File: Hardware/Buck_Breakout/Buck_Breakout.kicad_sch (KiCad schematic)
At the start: 7 parts, among them U1 AP62250WU

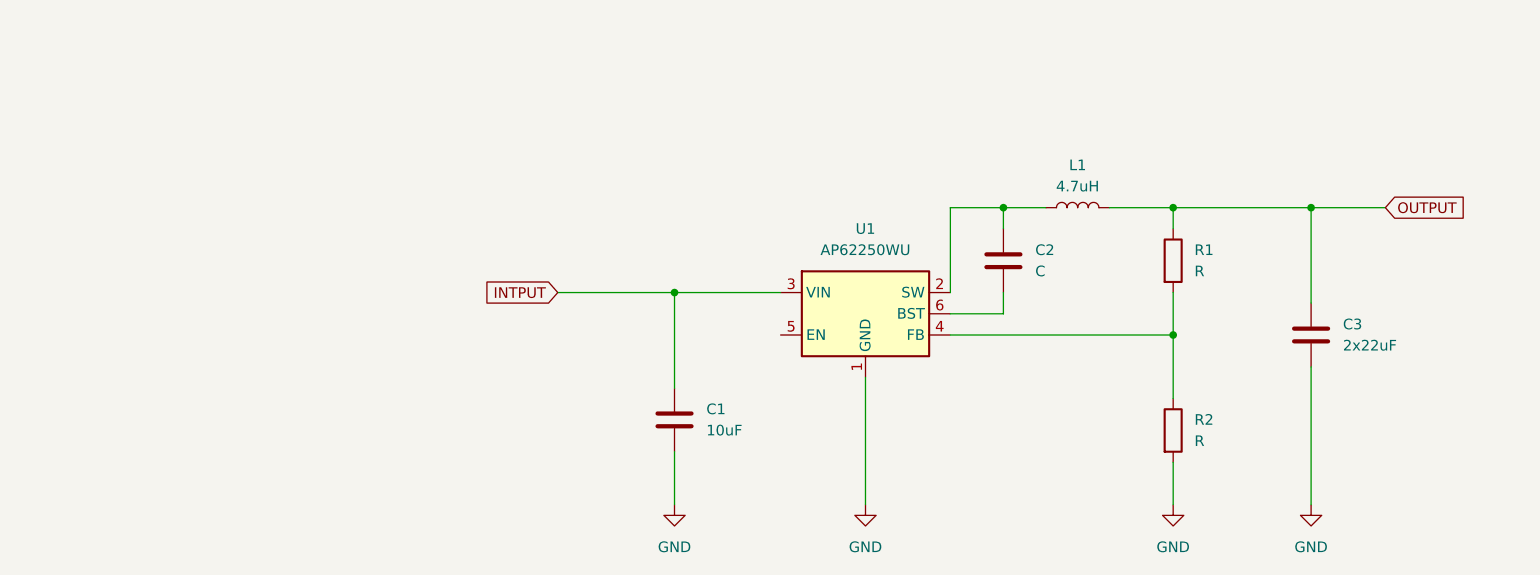
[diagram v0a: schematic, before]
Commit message: Finish Buck converter schematic and footprint assignments
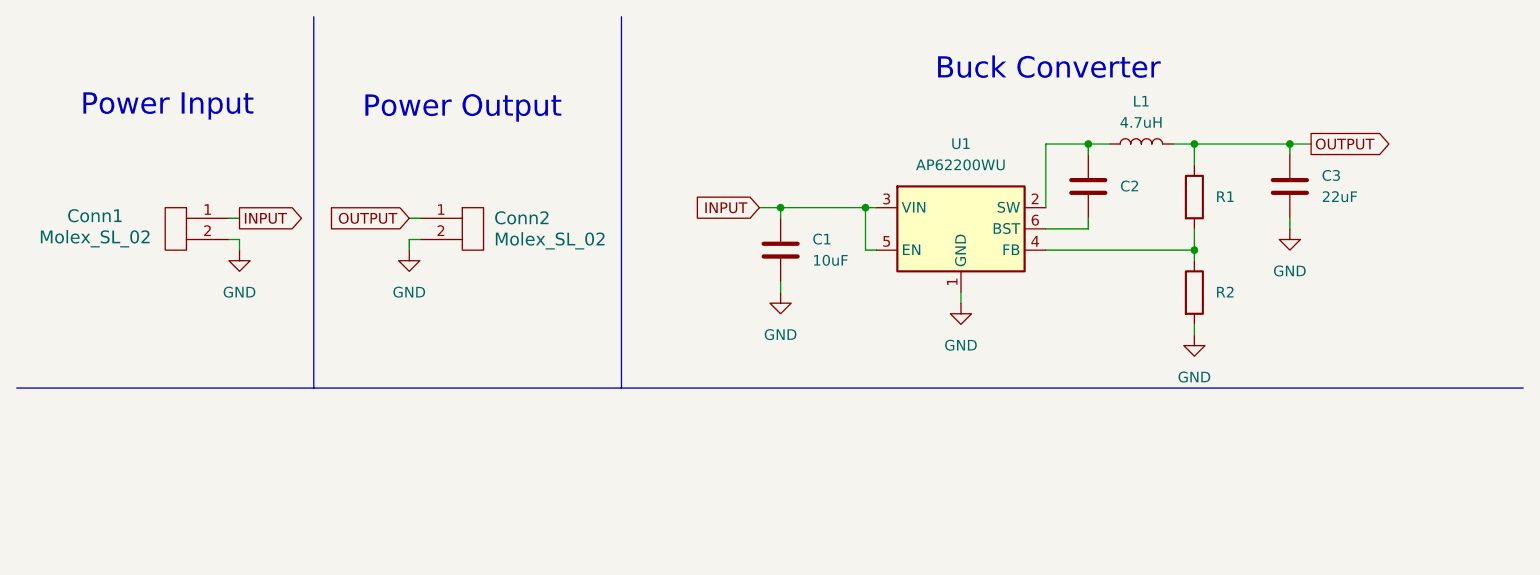
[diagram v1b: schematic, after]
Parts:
- added Conn1, Conn2: Molex_SL_02, MRDT_Connectors:MOLEX_SL_02_Vertical, symbol MRDT_Connectors:Molex_SL_02
- C1, C2: footprint (none) -> Capacitor_SMD:C_0603_1608Metric_Pad1.08x0.95mm_HandSolder
- C3: value 2x22uF -> 22uF; footprint (none) -> Capacitor_SMD:C_0603_1608Metric_Pad1.08x0.95mm_HandSolder
- L1: footprint (none) -> Inductor_SMD:L_1008_2520Metric_Pad1.43x2.20mm_HandSolder
- R1, R2: footprint (none) -> Resistor_SMD:R_0603_1608Metric_Pad0.98x0.95mm_HandSolder
- U1: value AP62250WU -> AP62200WU
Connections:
- net INTPUT is gone; now on net INPUT: C1.1, U1.3 (VIN)
- net GND: now also Conn1.2, Conn2.2
- net OUTPUT: now also Conn2.1
- net INPUT: now reaches U1.5 (EN)
- net INPUT: now also Conn1.1
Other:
- note added: "Buck Converter"
- note added: "Power Input"
- note added: "Power Output"
- moved on the sheet: C1, C2, C3, L1, R1, R2, U1

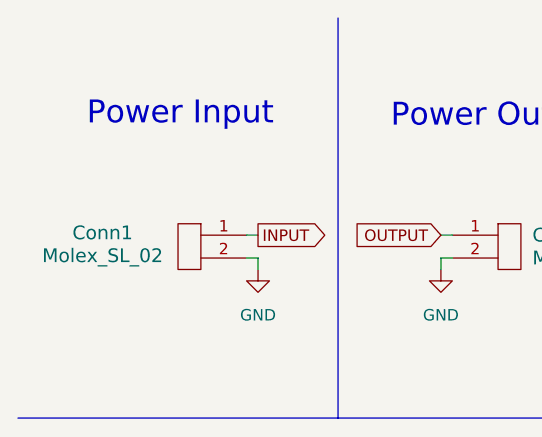
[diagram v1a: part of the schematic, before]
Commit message: Finish buck converter layout
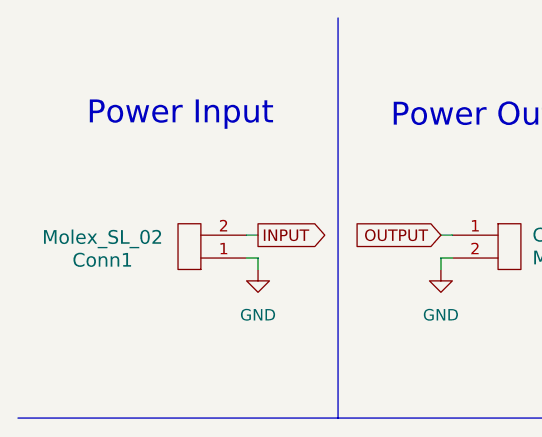
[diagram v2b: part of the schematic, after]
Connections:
- net GND: now also Conn1.1; no longer Conn1.2
- net INPUT: now also Conn1.2; no longer Conn1.1
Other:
- moved on the sheet: Conn1
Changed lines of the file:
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@@
 	(symbol
 		(lib_id "MRDT_Connectors:Molex_SL_02")
-		(at 31.75 39.37 0)
-		(mirror y)
+		(at 31.75 34.29 180)
 		(unit 1)
 		(exclude_from_sim no)
@@
 		(dnp no)
 		(property "Reference" "Conn1"
-			(at 20.828 35.306 0)
+			(at 20.828 38.354 0)
 			(effects
 				(font
@@
 		)
 		(property "Value" "Molex_SL_02"
-			(at 20.828 37.846 0)
+			(at 20.828 35.814 0)
 			(effects
 				(font
@@
 		)
 		(property "Footprint" "MRDT_Connectors:MOLEX_SL_02_Vertical"
-			(at 31.75 41.91 0)
+			(at 31.75 31.75 0)
 			(effects
 				(font
@@
 		)
 		(property "Datasheet" ""
-			(at 31.75 41.91 0)
+			(at 31.75 31.75 0)
 			(effects
 				(font
@@
 		)
 		(property "Description" ""
-			(at 31.75 39.37 0)
+			(at 31.75 34.29 0)
 			(effects
 				(font

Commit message: Generate BOM for buck breakout
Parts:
- C2: value C -> 100nF
- R1: value R -> R1
- R2: value R -> R2
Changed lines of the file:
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@@
 			)
 		)
-		(property "Value" "R"
+		(property "Value" "R2"
 			(at 154.94 45.7199 0)
 			(effects
@@
 		(on_board yes)
 		(dnp no)
-		(fields_autoplaced yes)
 		(property "Reference" "C2"
-			(at 143.51 31.7499 0)
-			(effects
-				(font
-					(size 1.27 1.27)
-				)
-				(justify left)
-			)
-		)
-		(property "Value" "C"
-			(at 143.51 33.0199 0)
-			(effects
-				(font
-					(size 1.27 1.27)
-				)
-				(justify left)
-				(hide yes)
+			(at 143.256 30.9879 0)
+			(effects
+				(font
+					(size 1.27 1.27)
+				)
+				(justify left)
+			)
+		)
+		(property "Value" "100nF"
+			(at 143.256 32.766 0)
+			(effects
+				(font
+					(size 1.27 1.27)
+				)
+				(justify left)
 			)
 		)
@@
 			)
 		)
-		(property "Value" "R"
+		(property "Value" "R1"
 			(at 154.94 34.2899 0)
 			(effects

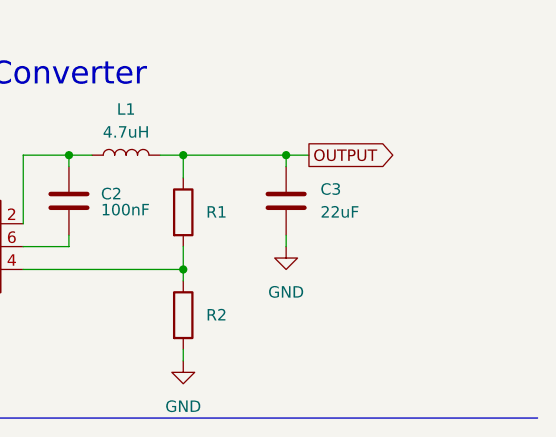
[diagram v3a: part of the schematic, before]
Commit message: Add second capacitor to buck breakout output
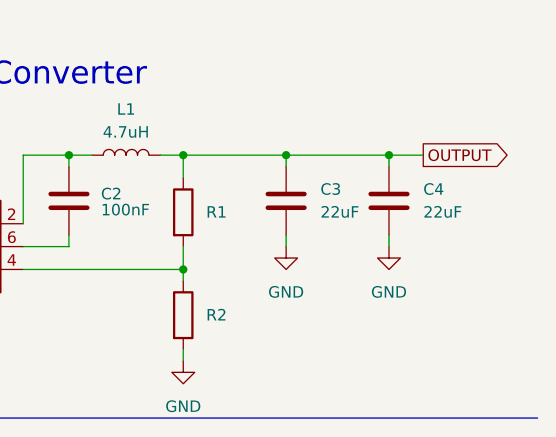
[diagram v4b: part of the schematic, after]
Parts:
- added C4: 22uF, Capacitor_SMD:C_0603_1608Metric_Pad1.08x0.95mm_HandSolder, symbol Device:C
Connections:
- net GND: now also C4.2
- net OUTPUT: now also C4.1
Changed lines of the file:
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@@
+	)
+	(junction
+		(at 175.26 26.67)
+		(diameter 0)
+		(color 0 0 0 0)
 	)
 	(junction
@@
 	(wire
 		(pts
-			(xy 163.83 26.67) (xy 166.37 26.67)
+			(xy 163.83 26.67) (xy 175.26 26.67)
 		)
 		(stroke
@@
 	(wire
 		(pts
+			(xy 175.26 27.94) (xy 175.26 26.67)
+		)
+		(stroke
+			(width 0)
+			(type default)
+		)
+	)
+	(wire
+		(pts
 			(xy 134.62 26.67) (xy 139.7 26.67)
 		)
@@
 	(wire
 		(pts
+			(xy 175.26 36.83) (xy 175.26 35.56)
+		)
+		(stroke
+			(width 0)
+			(type default)
+		)
+	)
+	(wire
+		(pts
 			(xy 152.4 39.37) (xy 152.4 40.64)
 		)
@@
 		(pts
 			(xy 36.83 38.1) (xy 38.1 38.1)
+		)
+		(stroke
+			(width 0)
+			(type default)
+		)
+	)
+	(wire
+		(pts
+			(xy 175.26 26.67) (xy 179.07 26.67)
 		)
 		(stroke
@@
 	(global_label "OUTPUT"
 		(shape output)
-		(at 166.37 26.67 0)
+		(at 179.07 26.67 0)
 		(fields_autoplaced yes)
 		(effects
@@
 		)
 		(property "Intersheetrefs" "${INTERSHEET_REFS}"
-			(at 176.5519 26.67 0)
+			(at 189.2519 26.67 0)
 			(effects
 				(font
@@
 	)
 	(symbol
+		(lib_id "Device:C")
+		(at 175.26 31.75 0)
+		(unit 1)
+		(exclude_from_sim no)
+		(in_bom yes)
+		(on_board yes)
+		(dnp no)
+		(fields_autoplaced yes)
+		(property "Reference" "C4"
+			(at 179.07 30.4799 0)
+			(effects
+				(font
+					(size 1.27 1.27)
+				)
+				(justify left)
+			)
+		)
+		(property "Value" "22uF"
+			(at 179.07 33.0199 0)
+			(effects
+				(font
+					(size 1.27 1.27)
+				)
+				(justify left)
+			)
+		)
+		(property "Footprint" "Capacitor_SMD:C_0603_1608Metric_Pad1.08x0.95mm_HandSolder"
+			(at 176.2252 35.56 0)
+			(effects
+				(font
+					(size 1.27 1.27)
+				)
+				(hide yes)
+			)
+		)
+		(property "Datasheet" "~"
+			(at 175.26 31.75 0)
+			(effects
+				(font
+					(size 1.27 1.27)
+				)
+				(hide yes)
+			)
+		)
+		(property "Description" "Unpolarized capacitor"
+			(at 175.26 31.75 0)
+			(effects
+				(font
+					(size 1.27 1.27)
+				)
+				(hide yes)
+			)
+		)
+		(pin "1"
+		)
+		(pin "2"
+		)
+		(instances
+			(project "Buck_Breakout"
+				(path "/94f3a2ba-6c26-4497-b452-3ee58af33c55"
+					(reference "C4")
+					(unit 1)
+				)
+			)
+		)
+	)
+	(symbol
 		(lib_id "power:GND")
 		(at 124.46 45.72 0)
@@
 					(unit 1)
 				)
+			)
+		)
+	)
+	(symbol
+		(lib_id "power:GND")
+		(at 175.26 36.83 0)
+		(unit 1)
+		(exclude_from_sim no)
+		(in_bom yes)
+		(on_board yes)
+		(dnp no)
+		(fields_autoplaced yes)
+		(property "Reference" "#PWR07"
+			(at 175.26 43.18 0)
+			(effects
+				(font
+					(size 1.27 1.27)
+				)
+				(hide yes)
+			)
+		)
+		(property "Value" "GND"
+			(at 175.26 41.91 0)
+			(effects
+				(font
+					(size 1.27 1.27)
+				)
+			)
+		)
+		(property "Footprint" ""
+			(at 175.26 36.83 0)
+			(effects
+				(font
+					(size 1.27 1.27)
+				)
+				(hide yes)
+			)
+		)
+		(property "Datasheet" ""
+			(at 175.26 36.83 0)
+			(effects
+				(font
+					(size 1.27 1.27)
+				)
+				(hide yes)
+			)
+		)
+		(property "Description" "Power symbol creates a global label with name \"GND\" , ground"
+			(at 175.26 36.83 0)
+			(effects
+				(font
+					(size 1.27 1.27)
+				)
+				(hide yes)
+			)
+		)
+		(pin "1"
+		)
+		(instances
+			(project "Buck_Breakout"
+				(path "/94f3a2ba-6c26-4497-b452-3ee58af33c55"
+					(reference "#PWR07")
+					(unit 1)
+				)
